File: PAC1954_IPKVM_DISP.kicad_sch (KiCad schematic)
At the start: 9 parts, among them U30 UCS2113-1-V_G4

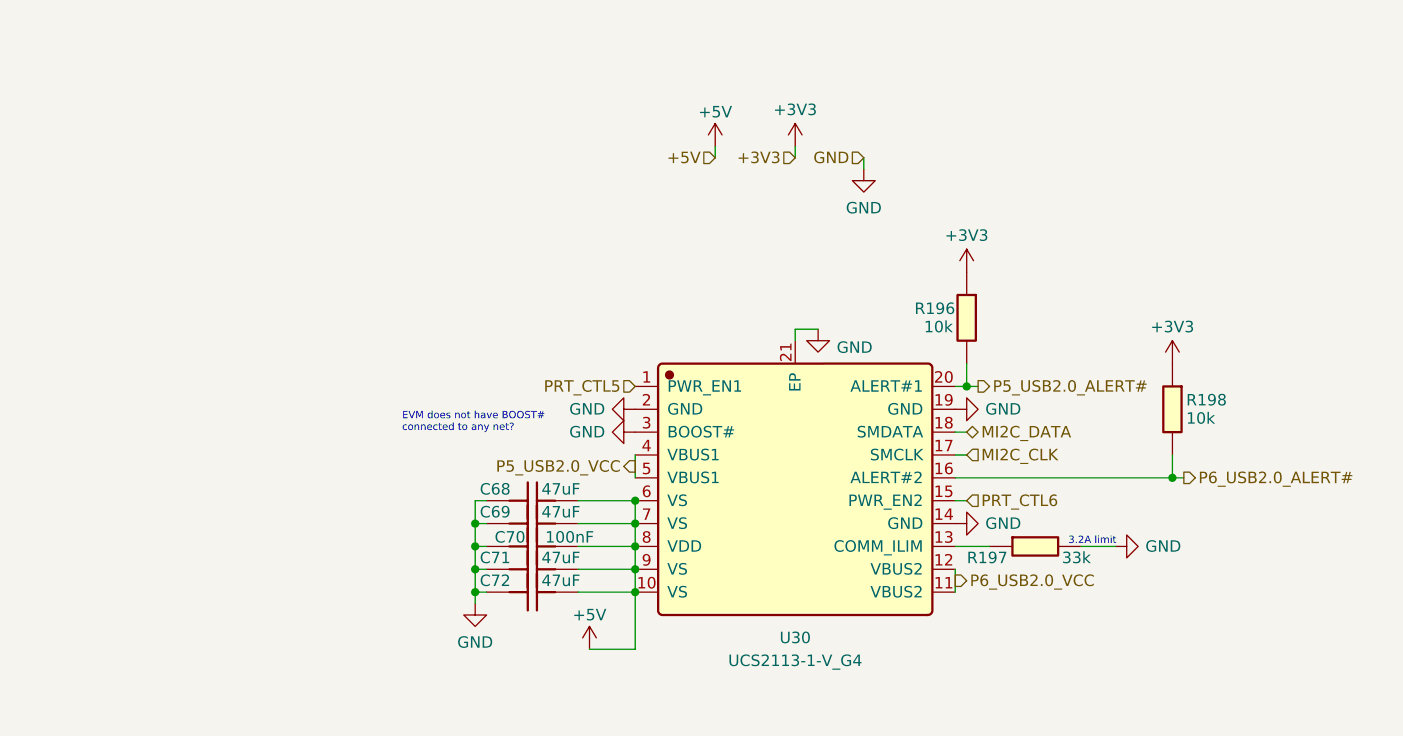
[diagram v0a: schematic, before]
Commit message: Transferred everything to hierarchical schematic and wired PSU power on circuit AND created duplicate schematics for all relevant subsystems
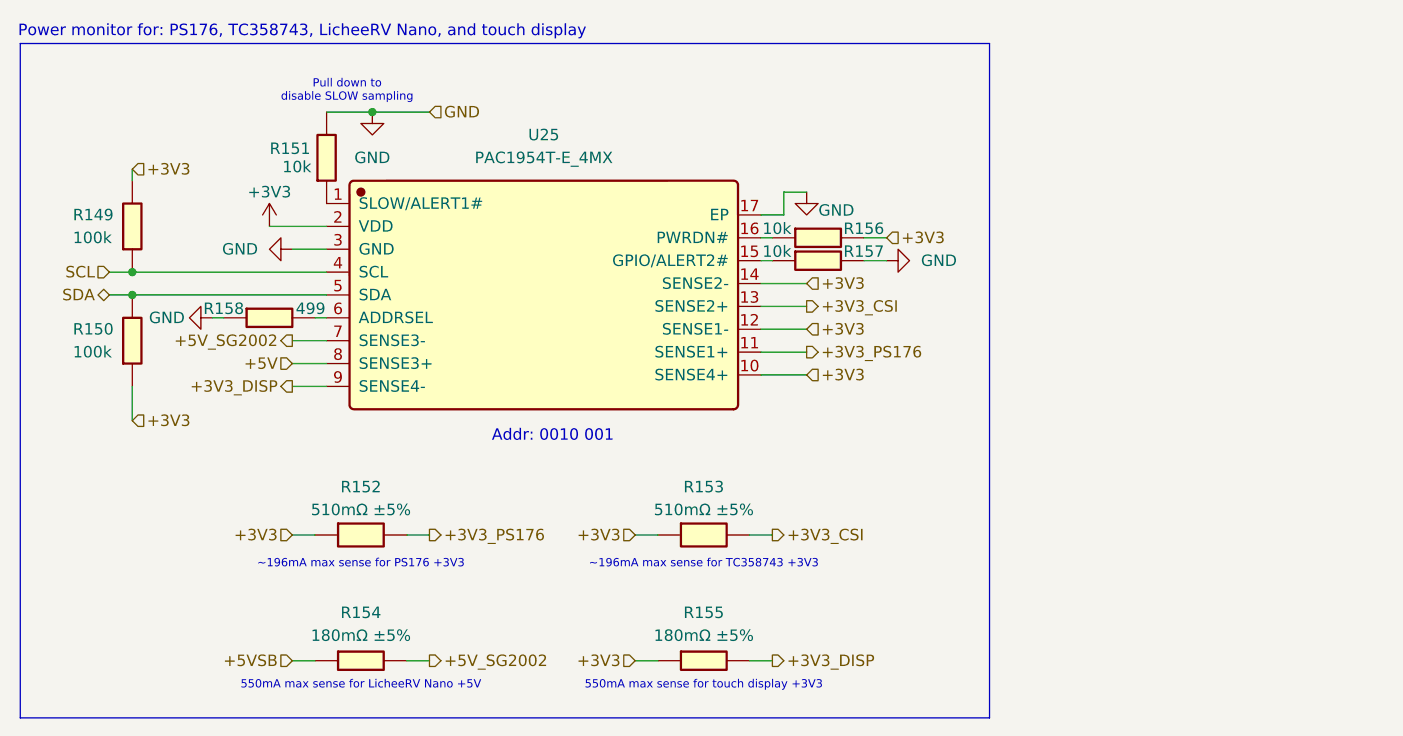
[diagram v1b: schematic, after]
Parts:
- removed C68, C69, C71, C72: 47uF, Capacitor_SMD:C_1206_3216Metric, symbol JLCImport:CL31A476MPHNNNE
- removed C70: 100nF, Capacitor_SMD:C_0402_1005Metric, symbol JLCImport:CL05B104KB54PNC
- removed R196, R198: 10k, Resistor_SMD:R_0402_1005Metric, symbol JLCImport:0402WGF1002TCE
- removed R197: 33k, Resistor_SMD:R_0402_1005Metric, symbol JLCImport:WR04X3302FTL
- removed U30: UCS2113-1-V_G4, JLCImport:UCS2113-1-V_G4, symbol JLCImport:UCS2113-1-V_G4
- added R149, R150: 100k, Resistor_SMD:R_0402_1005Metric, symbol JLCImport:0402WGF1003TCE
- added R151, R156, R157: 10k, Resistor_SMD:R_0402_1005Metric, symbol JLCImport:0402WGF1002TCE
- added R152, R153: 510mΩ ±5%, Resistor_SMD:R_1210_3225Metric, symbol JLCImport:YHR1206SE1WR003F5
- added R154, R155: 180mΩ ±5%, Resistor_SMD:R_0508_1220Metric, symbol JLCImport:LTR10EVHJLR18
- added R158: 499, Resistor_SMD:R_0402_1005Metric, symbol JLCImport:WR04W1R00FTL
- added U25: PAC1954T-E_4MX, JLCImport:PAC1954T-E_4MX, symbol JLCImport:PAC1954T-E_4MX
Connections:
- net +3V3: now also R149.2, R150.1, R152.1, R153.1, R155.1, R156.2, U25.10 (SENSE4+), U25.12 (SENSE1-), U25.14 (SENSE2-), U25.2 (VDD)
- net +5V: now also U25.8 (SENSE3+)
- net GND: now also R151.2, R157.2, R158.1, U25.17 (EP), U25.3 (GND)
- new net: R156.1, U25.16 (PWRDN#)
- new net: R158.2, U25.6 (ADDRSEL)
- new net: R157.1, U25.15 (GPIO/ALERT2#)
- new net: R151.1, U25.1 (SLOW/ALERT1#)
- new net +3V3_CSI: R153.2, U25.13 (SENSE2+)
- new net +3V3_DISP: R155.2, U25.9 (SENSE4-)
- new net +3V3_PS176: R152.2, U25.11 (SENSE1+)
- new net +5VSB: R154.1
- new net +5V_SG2002: R154.2, U25.7 (SENSE3-)
- new net SCL: R149.1, U25.4 (SCL)
- new net SDA: R150.2, U25.5 (SDA)
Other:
- note added: "550mA max sense for LicheeRV Nano +5V"
- note added: "550mA max sense for touch display +3V3"
- note added: "Addr: 0010 001"
- note added: "Power monitor for: PS176, TC358743, LicheeRV Nano, and touch display"
- note added: "Pull down to disable SLOW sampling"
- note added: "~196mA max sense for PS176 +3V3"
- note added: "~196mA max sense for TC358743 +3V3"
- note removed: "3.2A limit"
- note removed: "EVM does not have BOOST# connected to any net?"
